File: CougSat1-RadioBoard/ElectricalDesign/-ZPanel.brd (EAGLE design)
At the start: 96 x 96 mm, 50 parts, among them J1 High Gain Antenna, J2 Deployables, J3 High Gain +, J4 ADCS, J5 Flap +X, J6 Flap -X, J7 Flap +Y, J8 Flap -Y, U1 AD7291, U2 AD8542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

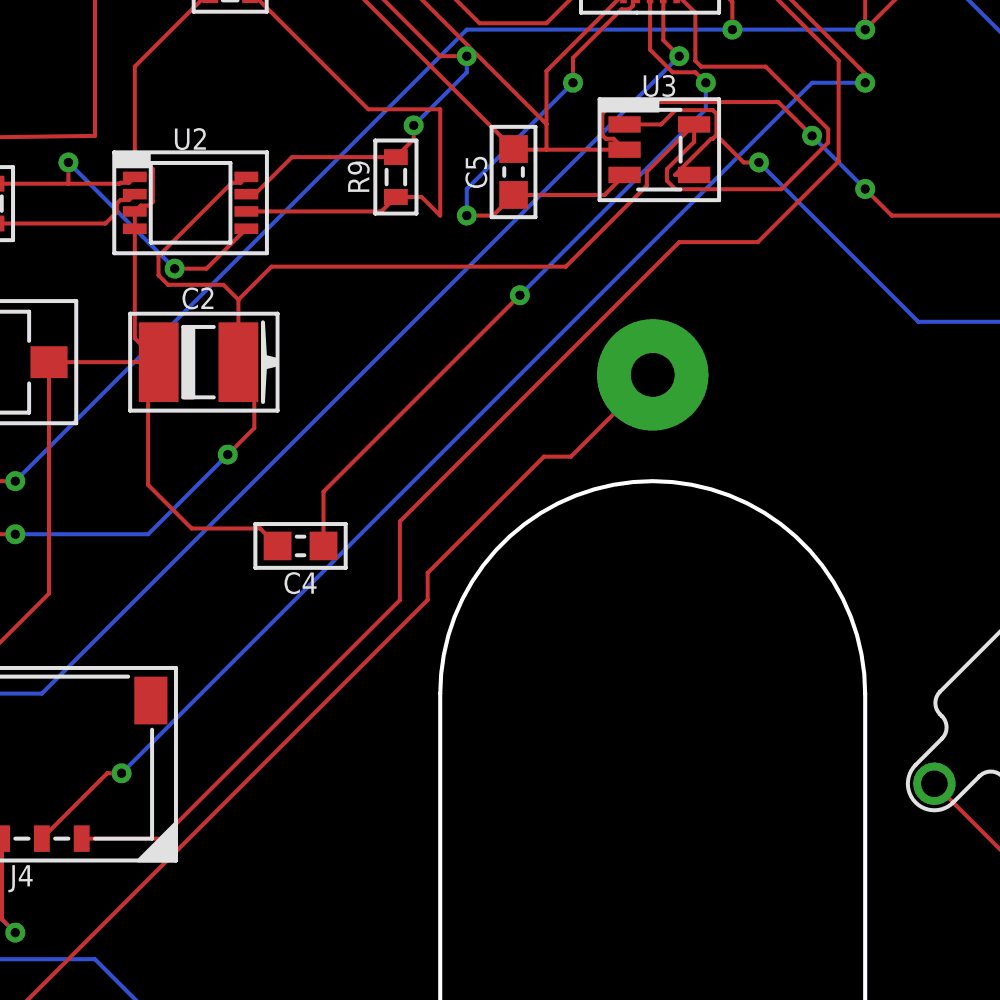
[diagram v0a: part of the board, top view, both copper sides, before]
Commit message: Revert "Layout 1.0.0"
This reverts commit 992a898be94d747baefa5f2d3c94eef64dce9a72.
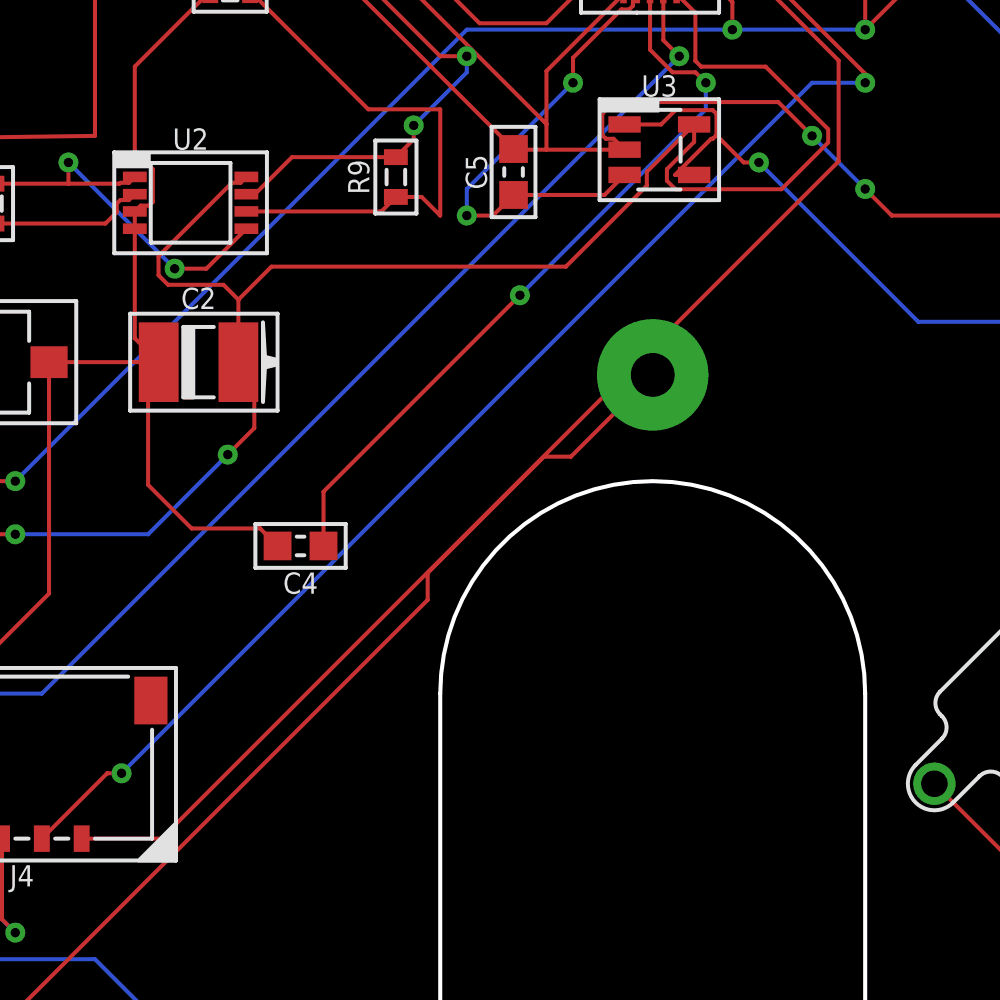
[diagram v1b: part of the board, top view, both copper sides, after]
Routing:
- net I2C_SDA_ADCS: track 51.8 -> 50.1 mm
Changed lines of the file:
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@@
 <contactref element="U1" pad="14"/>
 <contactref element="J4" pad="1"/>
-<wire x1="29.5" y1="56.54" x2="38.48" y2="65.52" width="0.1524" layer="1"/>
+<wire x1="55" y1="82.04" x2="29.5" y2="56.54" width="0.1524" layer="1"/>
 <wire x1="26.5" y1="56.54" x2="29.5" y2="56.54" width="0.1524" layer="1"/>
 <wire x1="50.2446875" y1="90.5936" x2="49.9464" y2="90.5936" width="0.1524" layer="1"/>
@@
 <wire x1="55" y1="85.8382875" x2="50.2446875" y2="90.5936" width="0.1524" layer="1"/>
 <wire x1="55" y1="82.04" x2="55" y2="85.8382875" width="0.1524" layer="1"/>
-<wire x1="38.48" y1="65.52" x2="38.48" y2="68.48" width="0.1524" layer="1"/>
-<wire x1="38.48" y1="68.48" x2="49" y2="79" width="0.1524" layer="1"/>
-<wire x1="49" y1="79" x2="51.96" y2="79" width="0.1524" layer="1"/>
-<wire x1="51.96" y1="79" x2="55" y2="82.04" width="0.1524" layer="1"/>
 </signal>
 <signal name="I2C_SCL_ADCS">
@@
 <wire x1="44.922309375" y1="70.922309375" x2="48" y2="74" width="0.1524" layer="1"/>
 <wire x1="39.526871875" y1="65.526871875" x2="39.526871875" y2="66.542471875" width="0.1524" layer="1"/>
-<wire x1="39.526871875" y1="66.542471875" x2="40.9922" y2="68.0078" width="0.1524" layer="1"/>
-<wire x1="40.9922" y1="68.0078" x2="43.906709375" y2="70.922309375" width="0.1524" layer="1"/>
+<wire x1="39.526871875" y1="66.542471875" x2="43.906709375" y2="70.922309375" width="0.1524" layer="1"/>
 <wire x1="43.906709375" y1="70.922309375" x2="44.922309375" y2="70.922309375" width="0.1524" layer="1"/>
 <wire x1="73.74" y1="47.48" x2="62.25" y2="28" width="0.1524" layer="1"/>

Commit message: Layout 1.0.0
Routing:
- net I2C_SDA_ADCS: track 50.1 -> 51.8 mm
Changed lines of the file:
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@@
 <contactref element="U1" pad="14"/>
 <contactref element="J4" pad="1"/>
-<wire x1="55" y1="82.04" x2="29.5" y2="56.54" width="0.1524" layer="1"/>
+<wire x1="29.5" y1="56.54" x2="38.48" y2="65.52" width="0.1524" layer="1"/>
 <wire x1="26.5" y1="56.54" x2="29.5" y2="56.54" width="0.1524" layer="1"/>
 <wire x1="50.2446875" y1="90.5936" x2="49.9464" y2="90.5936" width="0.1524" layer="1"/>
@@
 <wire x1="55" y1="85.8382875" x2="50.2446875" y2="90.5936" width="0.1524" layer="1"/>
 <wire x1="55" y1="82.04" x2="55" y2="85.8382875" width="0.1524" layer="1"/>
+<wire x1="38.48" y1="65.52" x2="38.48" y2="68.48" width="0.1524" layer="1"/>
+<wire x1="38.48" y1="68.48" x2="49" y2="79" width="0.1524" layer="1"/>
+<wire x1="49" y1="79" x2="51.96" y2="79" width="0.1524" layer="1"/>
+<wire x1="51.96" y1="79" x2="55" y2="82.04" width="0.1524" layer="1"/>
 </signal>
 <signal name="I2C_SCL_ADCS">
@@
 <wire x1="44.922309375" y1="70.922309375" x2="48" y2="74" width="0.1524" layer="1"/>
 <wire x1="39.526871875" y1="65.526871875" x2="39.526871875" y2="66.542471875" width="0.1524" layer="1"/>
-<wire x1="39.526871875" y1="66.542471875" x2="43.906709375" y2="70.922309375" width="0.1524" layer="1"/>
+<wire x1="39.526871875" y1="66.542471875" x2="40.9922" y2="68.0078" width="0.1524" layer="1"/>
+<wire x1="40.9922" y1="68.0078" x2="43.906709375" y2="70.922309375" width="0.1524" layer="1"/>
 <wire x1="43.906709375" y1="70.922309375" x2="44.922309375" y2="70.922309375" width="0.1524" layer="1"/>
 <wire x1="73.74" y1="47.48" x2="62.25" y2="28" width="0.1524" layer="1"/>
